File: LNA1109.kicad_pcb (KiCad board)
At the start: 4 copper layers, 11.7 x 8.7 mm, 25 parts, among them P1 SMA-KIT-1.5MF, U1 SWITCH, U2 SWITCH, U3 LNA, U4 SAW

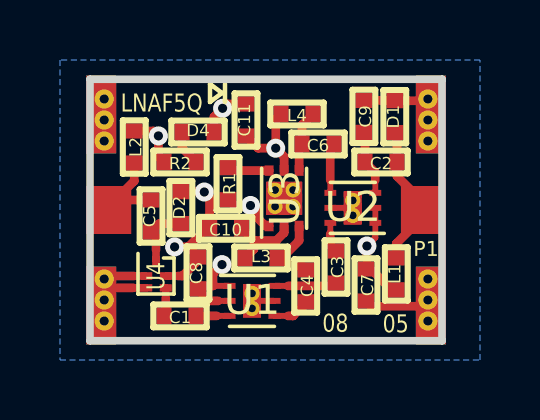
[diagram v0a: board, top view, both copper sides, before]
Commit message: rename from LNAF5Q to LNA1109
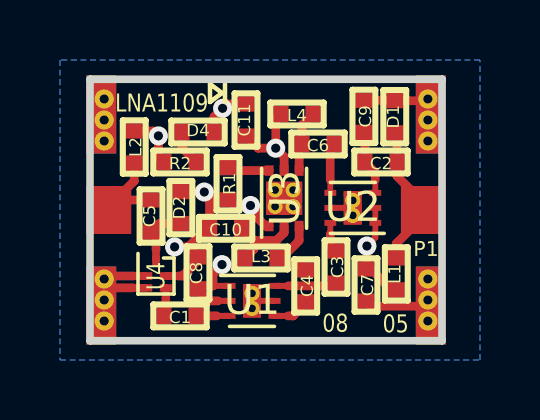
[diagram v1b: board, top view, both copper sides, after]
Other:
- board text added: "LNA1109"
- board text removed: "LNAF5Q"
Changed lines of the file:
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@@
   (page A4)
   (title_block
-    (title LNAF5Q)
+    (title LNA1109)
     (date 2020-08-05)
     (company "Copyright (c) 2014-2020 Great Scott Gadgets <info@greatscottgadgets.com>")
@@
     (effects (font (size 0.6 0.5) (thickness 0.1)))
   )
-  (gr_text LNAF5Q (at 132.72 96.74) (layer B.SilkS)
+  (gr_text LNA1109 (at 132.72 96.74) (layer B.SilkS)
     (effects (font (size 1.2 1) (thickness 0.2)) (justify mirror))
   )
@@
     (effects (font (size 0.6 0.5) (thickness 0.1)))
   )
-  (gr_text LNAF5Q (at 127.39 96.44) (layer F.SilkS)
+  (gr_text LNA1109 (at 127.39 96.44) (layer F.SilkS)
     (effects (font (size 0.6 0.5) (thickness 0.1)))
   )
